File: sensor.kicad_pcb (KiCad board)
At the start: 2 copper layers, 38.7 x 42.8 mm, 15 parts, among them J1 Conn_01x06, U1 TCR2EF19, U2 PMW3610

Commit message: routingrouting
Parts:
- removed ?: , 
- removed C4: 0.1u, Capacitor_SMD:C_0603_1608Metric
- removed C5: 1u, Capacitor_SMD:C_0603_1608Metric
- removed REF**: MountingHole_3.2mm_M3_ISO7380_Pad, MountingHole:MountingHole_3.2mm_M3_ISO7380_Pad
- removed U1: TCR2EF19, Package_TO_SOT_SMD:SOT-23-5
- added C10: 1uF, lib:C_0603_1608Metric, B.Cu at (87.4, 120.0)
- added C11: 1uF, lib:C_0603_1608Metric, B.Cu at (89.8, 115.8)
- added IC1: AP7335-WG-7, Package_TO_SOT_SMD:SOT-23-5_HandSoldering, B.Cu at (90.2, 119.0)
- added R2: 10k, lib:R_0603_1608Metric, B.Cu at (90.5, 122.2)
- added R3: 15k, lib:R_0603_1608Metric, B.Cu at (87.4, 122.2)
- J1: value Conn_01x06 -> Conn_01x08
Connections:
- J1 pad 1: VCC -> GND
- J1 pad 2: NCS_2 -> VCC
- J1 pad 3: SDIO_2 -> MOTION_2
- J1 pad 4: SCLK_2 -> SDIO_2
- J1 pad 5: MOTION_2 -> SCLK_2
- J1 pad 6: GND -> NCS_2
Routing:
- net +1V9: track 66.9 -> 19.3 mm
- net MOTION_2: track 63.8 -> 32.6 mm
- net Net-(U2-+VCSEL): track 42.3 -> 30.3 mm
- net SCLK_2: track 49.9 -> 39.3 mm
- net NCS_2: track 33.2 -> 40.8 mm, vias 1 -> 0
- net Net-(IC1-ADJ): track 0.00 -> 7.28 mm
- net GND: track 8.12 -> 13.0 mm, vias 2 -> 7
- net VCC: track 41.4 -> 45.8 mm, vias 0 -> 1
- net SDIO_2: track 43.1 -> 47.1 mm
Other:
- board text added: "todo: fonts, fira license // name on model // based on"

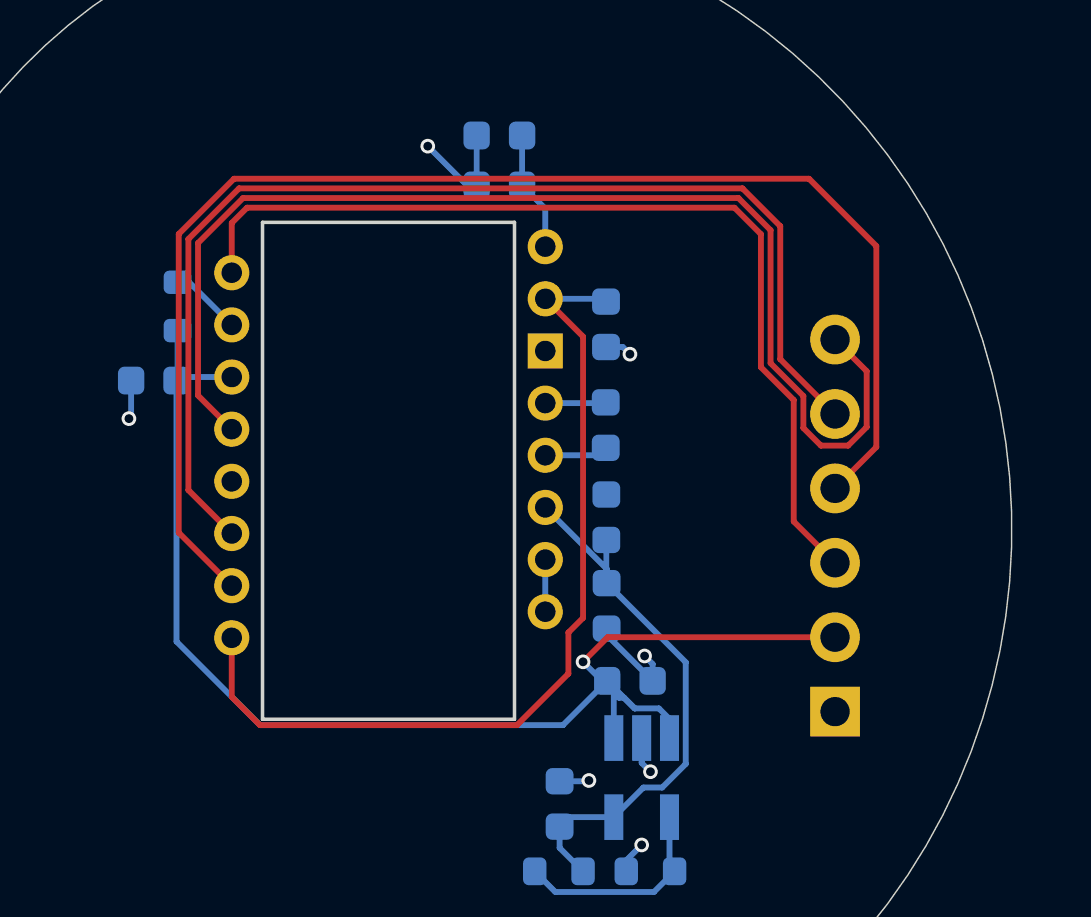
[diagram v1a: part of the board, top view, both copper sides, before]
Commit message: fix pinout routing, cleanup
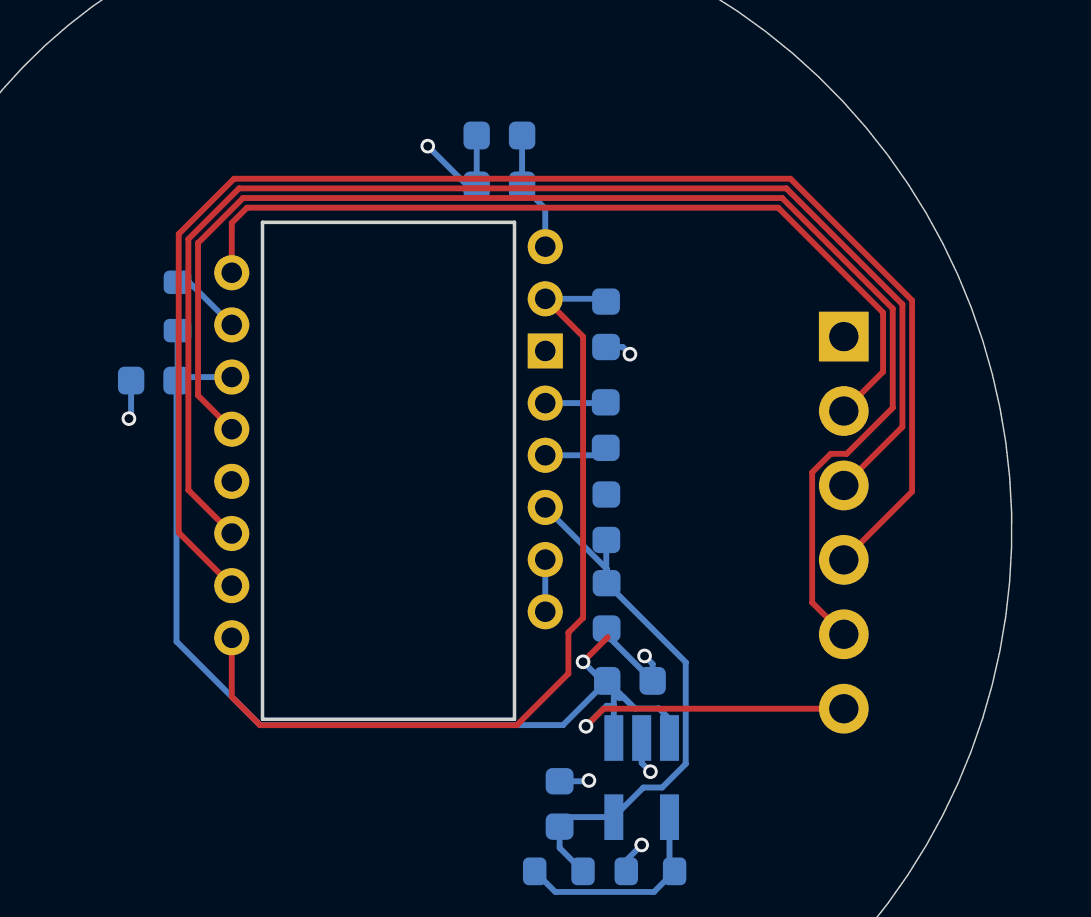
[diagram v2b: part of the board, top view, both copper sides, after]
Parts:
- moved J1 12.8 mm to (97.1, 104.0), turned to 0 degrees
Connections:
- J1 pad 2: VCC -> MOTION_2
- J1 pad 3: MOTION_2 -> SCLK_2
- J1 pad 5: SCLK_2 -> NCS_2
- J1 pad 6: NCS_2 -> VCC
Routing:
- net SCLK_2: track 39.3 -> 44.4 mm
- net NCS_2: track 40.8 -> 45.8 mm
- net MOTION_2: track 32.6 -> 29.5 mm
- net SDIO_2: track 47.1 -> 50.1 mm
- net VCC: track 45.8 -> 48.3 mm, vias 1 -> 2

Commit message: silkscreen
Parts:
- added G***: LOGO, LOGO, B.Cu at (67.6, 98.3)
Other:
- board text added: "CERN-OHL-S v2 Quentin Lebastard/BastardKB 2023 github.com/ufan 2022.09.04 voided 2023.03.16"
- board text added: "Charybdis PMW3610 adapter REV 1.0"
- board text added: "Install sensor oriented like this"
- board text added: "MO"
- board text removed: "MOTION"
- board text removed: "github.com/ufan 2022.09.04 voided 2023.03.16"

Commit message: routing, silkscreen
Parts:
- moved J1 2.30 mm to (99.4, 104.0)
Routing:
- net SDIO_2: track 50.1 -> 31.5 mm
- net SCLK_2: track 44.4 -> 34.6 mm
- net GND: track 13.0 -> 22.1 mm, vias 7 -> 9
- net VCC: track 48.3 -> 45.2 mm, vias 2 -> 1
- net MOTION_2: track 29.5 -> 30.9 mm

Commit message: placement
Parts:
- added ?: , , F.Cu at (81.6, 92.2)
- added ?: , , F.Cu at (81.6, 129.2)
- moved G*** 28.0 mm to (71.4, 126.1), turned to 140 degrees
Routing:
- net VCC: track 45.2 -> 48.2 mm
- net GND: track 22.1 -> 21.2 mm
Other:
- board text removed: "todo: fonts, fira license // name on model // based on"
